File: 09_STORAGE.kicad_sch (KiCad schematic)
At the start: 0 parts

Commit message: updated schematics
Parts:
- added C901: 4.7uF, Capacitor_SMD:C_0603_1608Metric, symbol Device:C
- added C902: 220nF, Capacitor_SMD:C_0402_1005Metric, symbol Device:C
- added C903: 2.2uF, Capacitor_SMD:C_0603_1608Metric, symbol Device:C
- added C904, C906: 100nF, Capacitor_SMD:C_0402_1005Metric, symbol Device:C
- added C905: 1.0uF, Capacitor_SMD:C_0402_1005Metric, symbol Device:C
- added R901: 10k, Resistor_SMD:R_0402_1005Metric, symbol Device:R
- added R902, R903, R904, R905, R906, R907, R908, R909, R910: 47k, Resistor_SMD:R_0402_1005Metric, symbol Device:R
- added U1: EMMC64G-TB9F-06011, symbol sportwatch_custom:EMMC64G-TB9F-06011
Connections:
- new net: U1.A1 (NC), U1.A10 (NC), U1.A11 (NC), U1.A12 (NC), U1.A13 (NC), U1.A14 (NC), U1.A2 (NC), U1.A7 (RFU), U1.A8 (NC), U1.A9 (NC), U1.B1 (NC), U1.B10 (NC), U1.B11 (NC), U1.B12 (NC), U1.B13 (NC), U1.B14 (NC), U1.B7 (NC), U1.B8 (NC), U1.B9 (NC), U1.C1 (NC), U1.C10 (NC), U1.C11 (NC), U1.C12 (NC), U1.C13 (NC), U1.C14 (NC), U1.C3 (NC), U1.C5 (NC), U1.C7 (NC), U1.C8 (NC), U1.C9 (NC), U1.D1 (NC), U1.D12 (NC), U1.D13 (NC), U1.D14 (NC), U1.D2 (NC), U1.D3 (NC), U1.D4 (NC), U1.E1 (NC), U1.E10 (VSF), U1.E12 (NC), U1.E13 (NC), U1.E14 (NC), U1.E2 (NC), U1.E3 (NC), U1.E5 (RFU), U1.E8 (VSF), U1.E9 (VSF), U1.F1 (NC), U1.F10 (VSF), U1.F12 (NC), U1.F13 (NC), U1.F14 (NC), U1.F2 (NC), U1.F3 (NC), U1.G1 (NC), U1.G10 (VSF), U1.G12 (NC), U1.G13 (NC), U1.G14 (NC), U1.G2 (NC), U1.G3 (RFU), U1.H1 (NC), U1.H12 (NC), U1.H13 (NC), U1.H14 (NC), U1.H2 (NC), U1.H3 (NC), U1.J1 (NC), U1.J12 (NC), U1.J13 (NC), U1.J14 (NC), U1.J2 (NC), U1.J3 (NC), U1.K1 (NC), U1.K10 (VSF), U1.K12 (NC), U1.K13 (NC), U1.K14 (NC), U1.K2 (NC), U1.K3 (NC), U1.K6 (RFU), U1.K7 (RFU), U1.L1 (NC), U1.L12 (NC), U1.L13 (NC), U1.L14 (NC), U1.L2 (NC), U1.L3 (NC), U1.M1 (NC), U1.M10 (NC), U1.M11 (NC), U1.M12 (NC), U1.M13 (NC), U1.M14 (NC), U1.M2 (NC), U1.M3 (NC), U1.M7 (NC), U1.M8 (NC), U1.M9 (NC), U1.N1 (NC), U1.N10 (NC), U1.N11 (NC), U1.N12 (NC), U1.N13 (NC), U1.N14 (NC), U1.N3 (NC), U1.N6 (NC), U1.N7 (NC), U1.N8 (NC), U1.N9 (NC), U1.P1 (NC), U1.P10 (RFU), U1.P11 (NC), U1.P12 (NC), U1.P13 (NC), U1.P14 (NC), U1.P2 (NC), U1.P7 (RFU), U1.P8 (NC), U1.P9 (NC)
- new net: U1.A6 (VSS), U1.P6 (VSSQ)
- new net EMMC_CLK: U1.M6 (CLK)
- new net EMMC_CMD: R901.2, U1.M5 (CMD)
- new net EMMC_DAT0: R902.2, U1.A3 (DAT0)
- new net EMMC_DAT1: R903.2, U1.A4 (DAT1)
- new net EMMC_DAT2: R904.2, U1.A5 (DAT2)
- new net EMMC_DAT3: R905.2, U1.B2 (DAT3)
- new net EMMC_DAT4: R906.2, U1.B3 (DAT4)
- new net EMMC_DAT5: R907.2, U1.B4 (DAT5)
- new net EMMC_DAT6: R908.2, U1.B5 (DAT6)
- new net EMMC_DAT7: R909.2, U1.B6 (DAT7)
- new net EMMC_RST_N: R910.2, U1.K5 (~{RST_n})
- new net EMMC_VDDI: C905.1, C906.1, U1.C2 (VDDI)
- new net GND: C901.2, C902.2, C903.2, C904.2, C905.2, C906.2, U1.K8 (VSS)
- new net VOUT1_1V8: C903.1, C904.1, R901.1, R910.1, U1.C6 (VCCQ), U1.N4 (VCCQ), U1.P5 (VCCQ)
- new net VOUT2_3V0_PROVISIONAL: C901.1, C902.1, U1.E6 (VCC), U1.K9 (VCC)
- no-connect marks 0 -> 1
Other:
- note added: "09_STORAGE — 64 GB eMMC / APOLLO510B SDIO0 8-BIT — REV A"
- note added: "Add/tune a small CLK source-series resistor near Apollo during 01_APOLLO integration (22 ohm initial target); keep it physically at the host, not beside U1."
- note added: "Apollo510B documents SDIO0 up to 96 MHz / 96 MB/s. Therefore U1 is NOT operated in HS400; H5/DS is intentionally NC."
- note added: "Architecture: Apollo510B SDIO0 is reserved for this eMMC because SDIO0 supports the full 8-bit eMMC bus."
- note added: "C901/C902: VCC 4.7uF + 220nF. C903/C904: VCCQ 2.2uF + 100nF. C905/C906: VDDI 1uF + 100nF."
- note added: "EMMC_RST_N uses a normal Apollo GPIO; hardware reset is disabled by default in eMMC and must be enabled through EXT_CSD if used."
- note added: "Kingston states DAT1-DAT7 internal pull-ups are disconnected after entering wide-bus modes, so external biasing remains useful."
- note added: "Kingston's public datasheet calls for an external VDDI Creg but refers exact design values to a separate design guide; capacitor values use standard eMMC guidance."
- note added: "Place U1 close to Apollo. Route CLK/CMD/DAT0..7 as controlled-impedance short traces with a continuous reference plane; length/skew review occurs in PCB phase."
- note added: "R901=10k CMD pull-up; R902-R909=47k DAT pull-ups; R910=47k reset pull-up. Values are conservative eMMC/JEDEC-style biasing."
- note added: "RFU/VSF/NC balls remain unconnected exactly as Kingston requires. Footprint is intentionally still unassigned pending the dedicated FBGA153 footprint audit."
- note added: "Reserve Apollo SDIF0 signals: DAT0..3 on GPIO84..87, CLK on GPIO88, DAT4..7 on GPIO156..159, CMD on GPIO160."
- note added: "U1 custom FBGA153 ball map verified against Kingston Table 9 before wiring."
- note added: "VCC = VOUT2_3V0_PROVISIONAL. Kingston allows 2.7-3.6 V; 3.0 V reduces load on the separate display 3.3 V rail."
- note added: "VCCQ = VOUT1_1V8. This keeps the complete SDIO0 bus in the 1.8 V I/O domain and preserves high-speed compatibility."
- note added: "VOUT rails and host labels are still local to this child sheet until final hierarchical integration."
- title: (none) -> Rev-A — 64 GB eMMC Storage

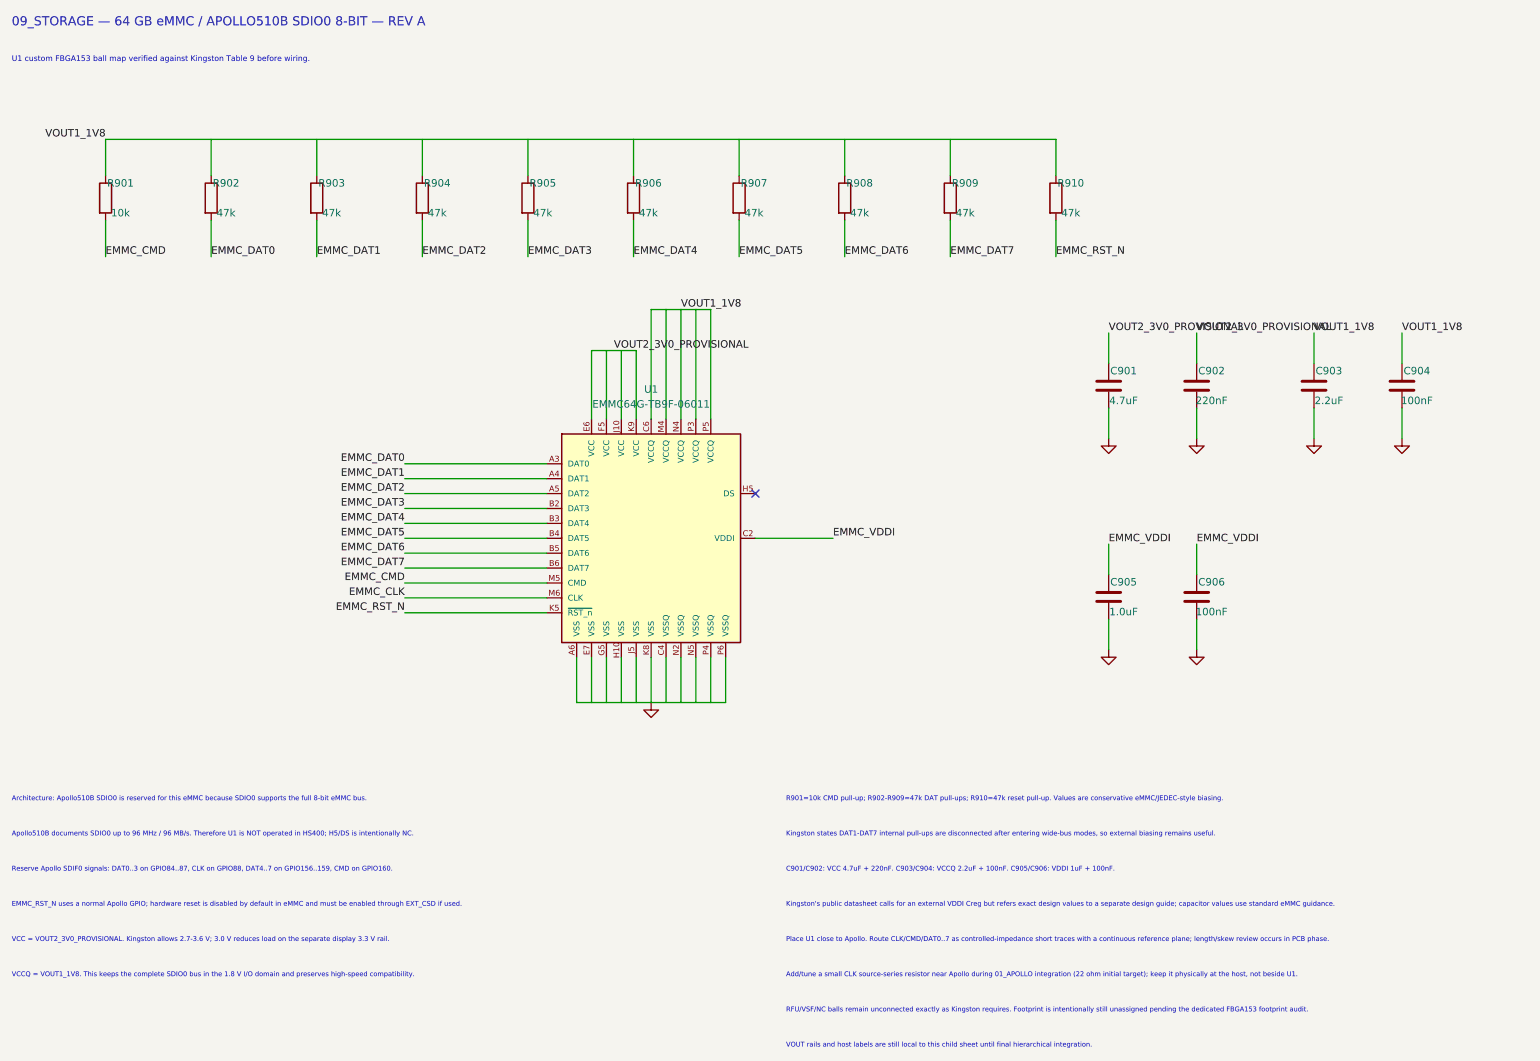
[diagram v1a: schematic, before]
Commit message: fixed schematics errors
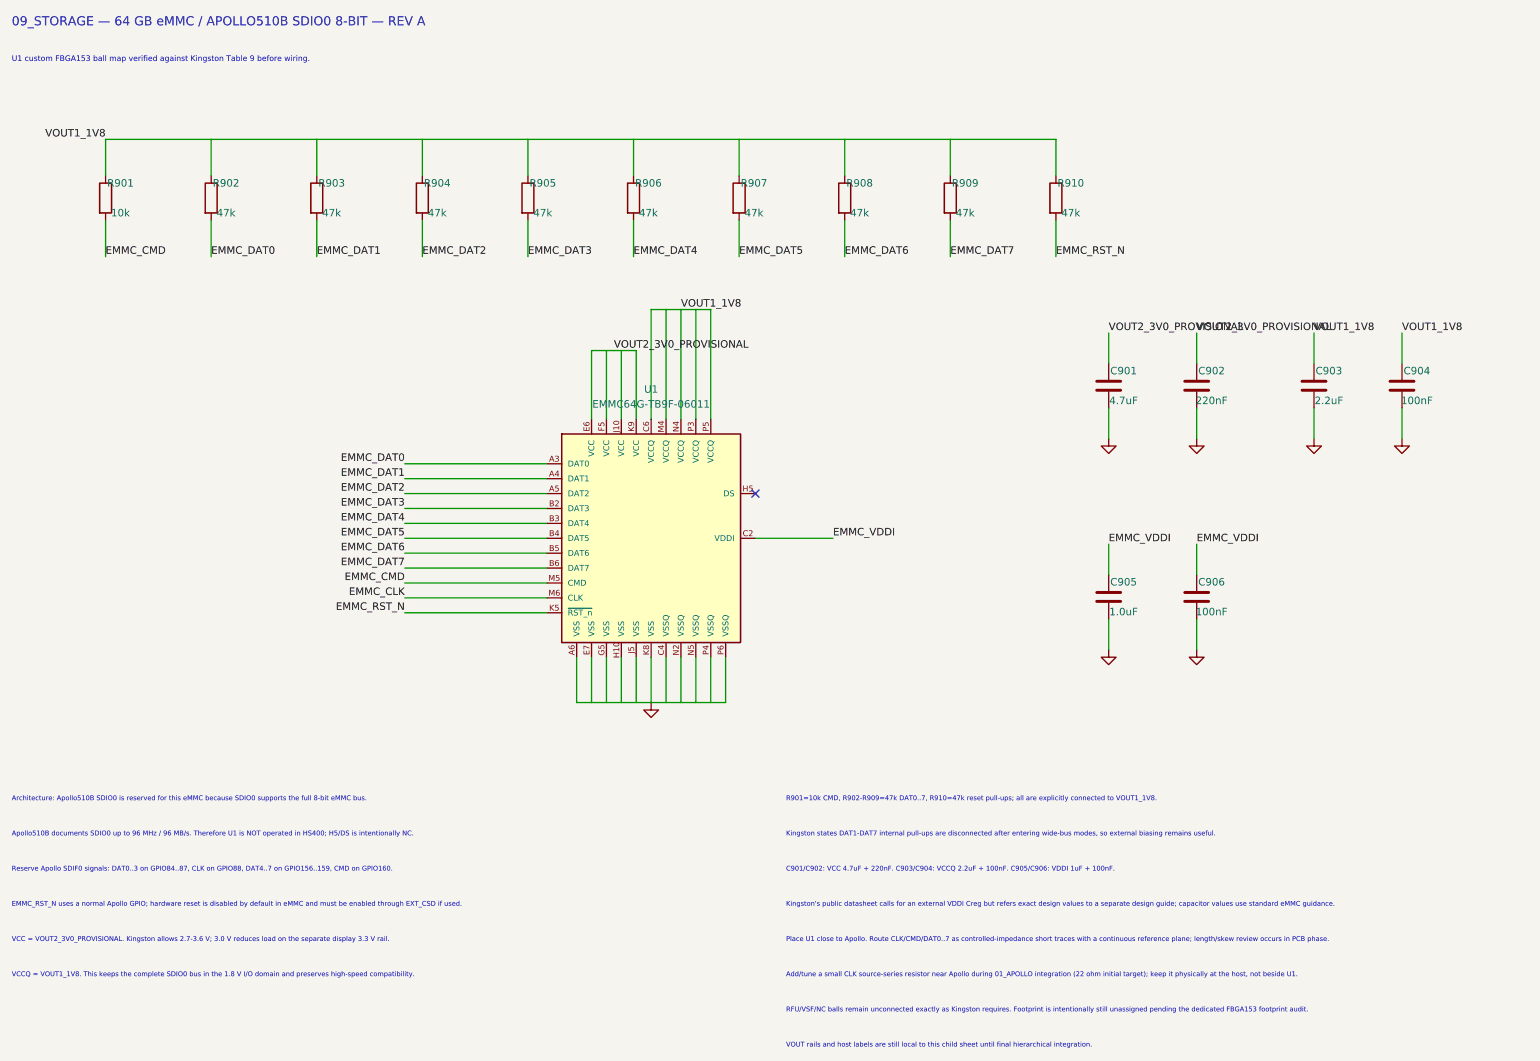
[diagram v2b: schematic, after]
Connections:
- net GND: now also U1.A6 (VSS), U1.C4 (VSSQ), U1.E7 (VSS), U1.G5 (VSS), U1.H10 (VSS), U1.J5 (VSS), U1.N2 (VSSQ), U1.N5 (VSSQ), U1.P4 (VSSQ), U1.P6 (VSSQ)
- net VOUT1_1V8: now also R902.1, R903.1, R904.1, R905.1, R906.1, R907.1, R908.1, R909.1, U1.M4 (VCCQ), U1.P3 (VCCQ)
- net VOUT2_3V0_PROVISIONAL: now also U1.F5 (VCC), U1.J10 (VCC)
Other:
- note added: "R901=10k CMD, R902-R909=47k DAT0..7, R910=47k reset pull-ups; all are explicitly connected to VOUT1_1V8."
- note removed: "R901=10k CMD pull-up; R902-R909=47k DAT pull-ups; R910=47k reset pull-up. Values are conservative eMMC/JEDEC-style biasing."
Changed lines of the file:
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@@
 		)
 	)
-	(text "R901=10k CMD pull-up; R902-R909=47k DAT pull-ups; R910=47k reset pull-up. Values are conservative eMMC/JEDEC-style biasing."
+	(text "R901=10k CMD, R902-R909=47k DAT0..7, R910=47k reset pull-ups; all are explicitly connected to VOUT1_1V8."
 		(exclude_from_sim no)
 		(at 150 145 0)
@@
 	(wire
 		(pts
-			(xy 114.3 128) (xy 139.7 128)
+			(xy 114.3 128) (xy 116.84 128)
+		)
+		(stroke
+			(width 0)
+			(type default)
+		)
+	)
+	(wire
+		(pts
+			(xy 116.84 128) (xy 119.38 128)
+		)
+		(stroke
+			(width 0)
+			(type default)
+		)
+	)
+	(wire
+		(pts
+			(xy 119.38 128) (xy 121.92 128)
+		)
+		(stroke
+			(width 0)
+			(type default)
+		)
+	)
+	(wire
+		(pts
+			(xy 121.92 128) (xy 124.46 128)
+		)
+		(stroke
+			(width 0)
+			(type default)
+		)
+	)
+	(wire
+		(pts
+			(xy 124.46 128) (xy 127 128)
+		)
+		(stroke
+			(width 0)
+			(type default)
+		)
+	)
+	(wire
+		(pts
+			(xy 127 128) (xy 129.54 128)
+		)
+		(stroke
+			(width 0)
+			(type default)
+		)
+	)
+	(wire
+		(pts
+			(xy 129.54 128) (xy 132.08 128)
+		)
+		(stroke
+			(width 0)
+			(type default)
+		)
+	)
+	(wire
+		(pts
+			(xy 132.08 128) (xy 134.62 128)
+		)
+		(stroke
+			(width 0)
+			(type default)
+		)
+	)
+	(wire
+		(pts
+			(xy 134.62 128) (xy 137.16 128)
+		)
+		(stroke
+			(width 0)
+			(type default)
+		)
+	)
+	(wire
+		(pts
+			(xy 137.16 128) (xy 139.7 128)
 		)
 		(stroke
@@
 	(wire
 		(pts
-			(xy 116.84 68) (xy 124.46 68)
+			(xy 116.84 68) (xy 119.38 68)
+		)
+		(stroke
+			(width 0)
+			(type default)
+		)
+	)
+	(wire
+		(pts
+			(xy 119.38 68) (xy 120.65 68)
+		)
+		(stroke
+			(width 0)
+			(type default)
+		)
+	)
+	(wire
+		(pts
+			(xy 120.65 68) (xy 121.92 68)
+		)
+		(stroke
+			(width 0)
+			(type default)
+		)
+	)
+	(wire
+		(pts
+			(xy 121.92 68) (xy 124.46 68)
 		)
 		(stroke
@@
 	(wire
 		(pts
-			(xy 127 61) (xy 137.16 61)
-		)
-		(stroke
-			(width 0)
-			(type default)
-		)
-	)
-	(wire
-		(pts
-			(xy 34 32) (xy 196 32)
-		)
-		(stroke
+			(xy 127 61) (xy 129.54 61)
+		)
+		(stroke
+			(width 0)
+			(type default)
+		)
+	)
+	(wire
+		(pts
+			(xy 129.54 61) (xy 132.08 61)
+		)
+		(stroke
+			(width 0)
+			(type default)
+		)
+	)
+	(wire
+		(pts
+			(xy 132.08 61) (xy 134.62 61)
+		)
+		(stroke
+			(width 0)
+			(type default)
+		)
+	)
+	(wire
+		(pts
+			(xy 134.62 61) (xy 137.16 61)
+		)
+		(stroke
+			(width 0)
+			(type default)
+		)
+	)
+	(wire
+		(pts
+			(xy 34 32) (xy 52 32)
+		)
+		(stroke
+			(width 0)
+			(type default)
+		)
+	)
+	(wire
+		(pts
+			(xy 52 32) (xy 70 32)
+		)
+		(stroke
+			(width 0)
+			(type default)
+		)
+	)
+	(wire
+		(pts
+			(xy 70 32) (xy 88 32)
+		)
+		(stroke
+			(width 0)
+			(type default)
+		)
+	)
+	(wire
+		(pts
+			(xy 88 32) (xy 106 32)
+		)
+		(stroke
+			(width 0)
+			(type default)
+		)
+	)
+	(wire
+		(pts
+			(xy 106 32) (xy 124 32)
+		)
+		(stroke
+			(width 0)
+			(type default)
+		)
+	)
+	(wire
+		(pts
+			(xy 124 32) (xy 142 32)
+		)
+		(stroke
+			(width 0)
+			(type default)
+		)
+	)
+	(wire
+		(pts
+			(xy 142 32) (xy 160 32)
+		)
+		(stroke
+			(width 0)
+			(type default)
+		)
+	)
+	(wire
+		(pts
+			(xy 160 32) (xy 178 32)
+		)
+		(stroke
+			(width 0)
+			(type default)
+		)
+	)
+	(wire
+		(pts
+			(xy 178 32) (xy 196 32)
+		)
+		(stroke

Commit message: refactor(kicad): integrate Rev-A hierarchy and libraries
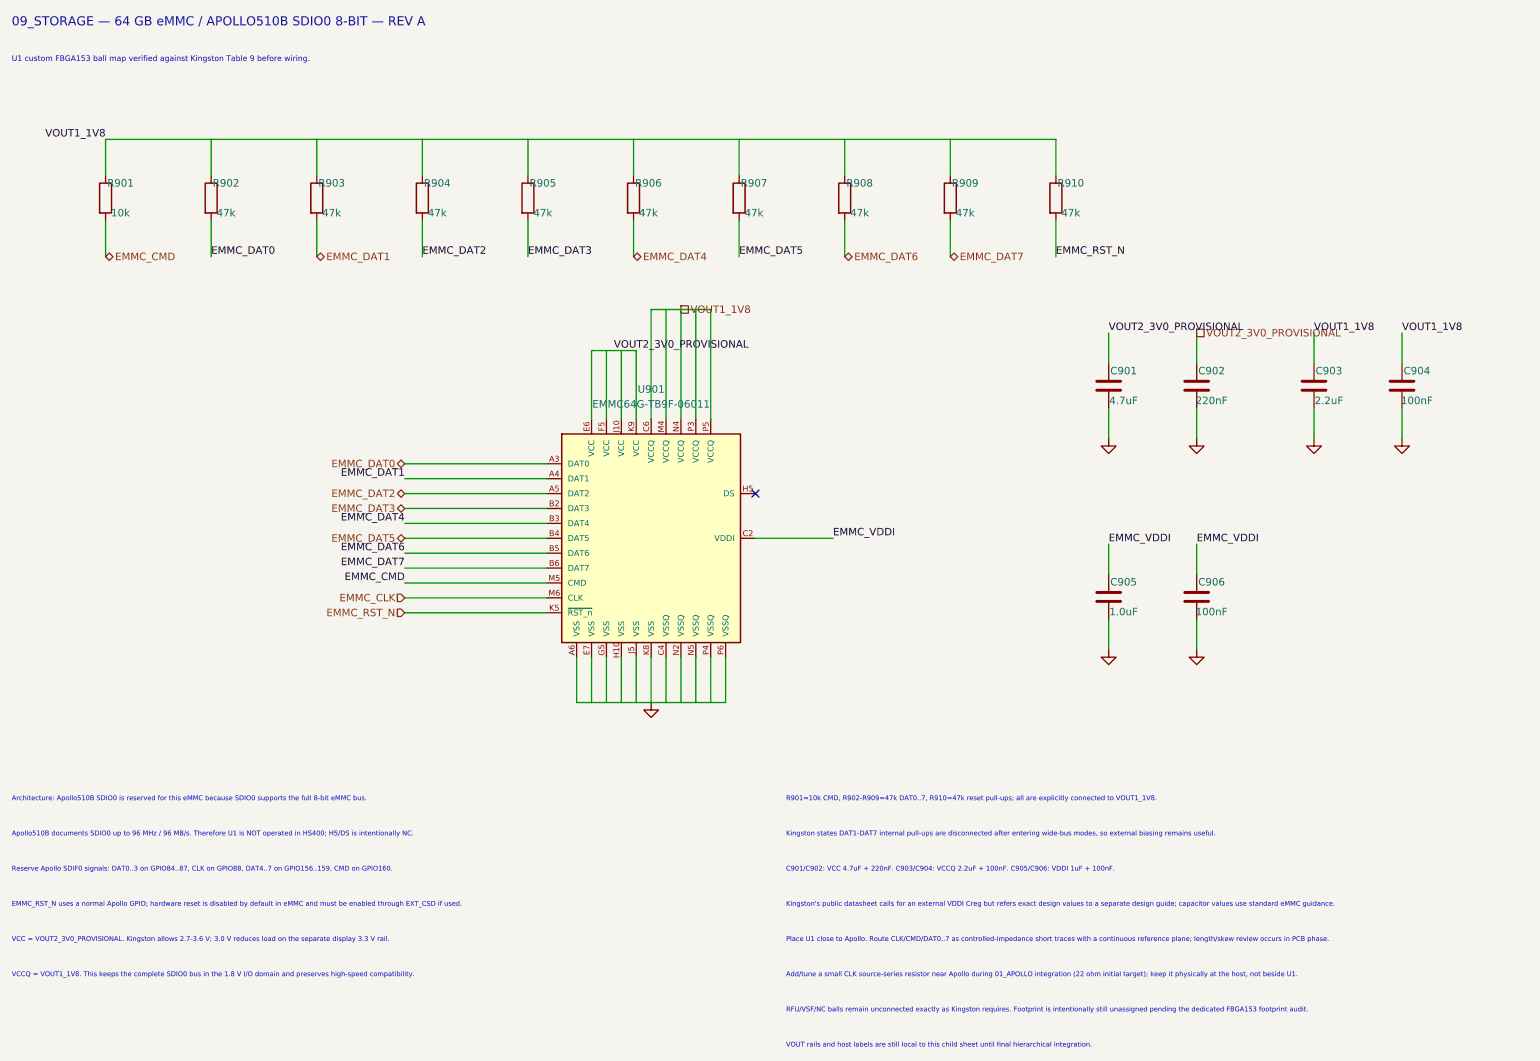
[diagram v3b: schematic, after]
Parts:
- renumbered U1 to U901
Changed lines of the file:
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@@
 		)
 	)
-	(label "VOUT2_3V0_PROVISIONAL"
+	(hierarchical_label "VOUT2_3V0_PROVISIONAL"
+		(shape passive)
 		(at 220 65 0)
 		(effects
@@
 		)
 	)
-	(label "EMMC_DAT4"
+	(hierarchical_label "EMMC_DAT4"
+		(shape bidirectional)
 		(at 124 52 0)
 		(effects
@@
 		)
 	)
-	(label "EMMC_DAT3"
+	(hierarchical_label "EMMC_DAT3"
+		(shape bidirectional)
 		(at 85 94.92 180)
 		(effects
@@
 		)
 	)
-	(label "EMMC_DAT2"
+	(hierarchical_label "EMMC_DAT2"
+		(shape bidirectional)
 		(at 85 92.38 180)
 		(effects
@@
 		)
 	)
-	(label "VOUT1_1V8"
+	(hierarchical_label "VOUT1_1V8"
+		(shape passive)
 		(at 132.08 61 0)
 		(effects
@@
 		)
 	)
-	(label "EMMC_DAT6"
+	(hierarchical_label "EMMC_DAT6"
+		(shape bidirectional)
 		(at 160 52 0)
 		(effects
@@
 		)
 	)
-	(label "EMMC_CMD"
+	(hierarchical_label "EMMC_CMD"
+		(shape bidirectional)
 		(at 34 52 0)
 		(effects
@@
 		)
 	)
-	(label "EMMC_DAT1"
+	(hierarchical_label "EMMC_DAT1"
+		(shape bidirectional)
 		(at 70 52 0)
 		(effects
@@
 		)
 	)
-	(label "EMMC_CLK"
+	(hierarchical_label "EMMC_CLK"
+		(shape input)
 		(at 85 110.16 180)
 		(effects
@@
 		)
 	)
-	(label "EMMC_DAT7"
+	(hierarchical_label "EMMC_DAT7"
+		(shape bidirectional)
 		(at 178 52 0)
 		(effects
@@
 		)
 	)
-	(label "EMMC_DAT5"
+	(hierarchical_label "EMMC_DAT5"
+		(shape bidirectional)
 		(at 85 100 180)
 		(effects
@@
 		)
 	)
-	(label "EMMC_RST_N"
+	(hierarchical_label "EMMC_RST_N"
+		(shape input)
 		(at 85 112.7 180)
 		(effects
@@
 		)
 	)
-	(label "EMMC_DAT0"
+	(hierarchical_label "EMMC_DAT0"
+		(shape bidirectional)
 		(at 85 87.3 180)
 		(effects
@@
 		(dnp no)
 		(fields_autoplaced yes)
-		(property "Reference" "U1"
+		(property "Reference" "U901"
 			(at 127 74.6 0)
 			(show_name no)
@@
 			(project "sportwatch_revA"
 				(path "/063f9d99-6c07-44cf-ba32-e33897e06972/a2d513ee-2f0e-4cad-81f9-7e29d5a45fba"
-					(reference "U1")
+					(reference "U901")
 					(unit 1)
 				)
@@
 			(project "09_STORAGE"
 				(path "/e1def6b6-01b4-4b57-bf23-17fd4247972f"
-					(reference "U1")
+					(reference "U901")
 					(unit 1)
 				)

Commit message: fix(kicad): correct PPG tri-state and eMMC hidden pins
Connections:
- now unconnected: U901.A1 (NC), U901.A10 (NC), U901.A11 (NC), U901.A12 (NC), U901.A13 (NC), U901.A14 (NC), U901.A2 (NC), U901.A7 (RFU), U901.A8 (NC), U901.A9 (NC), U901.B1 (NC), U901.B10 (NC), U901.B11 (NC), U901.B12 (NC), U901.B13 (NC), U901.B14 (NC), U901.B7 (NC), U901.B8 (NC), U901.B9 (NC), U901.C1 (NC), U901.C10 (NC), U901.C11 (NC), U901.C12 (NC), U901.C13 (NC), U901.C14 (NC), U901.C3 (NC), U901.C5 (NC), U901.C7 (NC), U901.C8 (NC), U901.C9 (NC), U901.D1 (NC), U901.D12 (NC), U901.D13 (NC), U901.D14 (NC), U901.D2 (NC), U901.D3 (NC), U901.D4 (NC), U901.E1 (NC), U901.E10 (VSF), U901.E12 (NC), U901.E13 (NC), U901.E14 (NC), U901.E2 (NC), U901.E3 (NC), U901.E5 (RFU), U901.E8 (VSF), U901.E9 (VSF), U901.F1 (NC), U901.F10 (VSF), U901.F12 (NC), U901.F13 (NC), U901.F14 (NC), U901.F2 (NC), U901.F3 (NC), U901.G1 (NC), U901.G10 (VSF), U901.G12 (NC), U901.G13 (NC), U901.G14 (NC), U901.G2 (NC), U901.G3 (RFU), U901.H1 (NC), U901.H12 (NC), U901.H13 (NC), U901.H14 (NC), U901.H2 (NC), U901.H3 (NC), U901.J1 (NC), U901.J12 (NC), U901.J13 (NC), U901.J14 (NC), U901.J2 (NC), U901.J3 (NC), U901.K1 (NC), U901.K10 (VSF), U901.K12 (NC), U901.K13 (NC), U901.K14 (NC), U901.K2 (NC), U901.K3 (NC), U901.K6 (RFU), U901.K7 (RFU), U901.L1 (NC), U901.L12 (NC), U901.L13 (NC), U901.L14 (NC), U901.L2 (NC), U901.L3 (NC), U901.M1 (NC), U901.M10 (NC), U901.M11 (NC), U901.M12 (NC), U901.M13 (NC), U901.M14 (NC), U901.M2 (NC), U901.M3 (NC), U901.M7 (NC), U901.M8 (NC), U901.M9 (NC), U901.N1 (NC), U901.N10 (NC), U901.N11 (NC), U901.N12 (NC), U901.N13 (NC), U901.N14 (NC), U901.N3 (NC), U901.N6 (NC), U901.N7 (NC), U901.N8 (NC), U901.N9 (NC), U901.P1 (NC), U901.P10 (RFU), U901.P11 (NC), U901.P12 (NC), U901.P13 (NC), U901.P14 (NC), U901.P2 (NC), U901.P7 (RFU), U901.P8 (NC), U901.P9 (NC)

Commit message: feat(kicad): assign and audit Rev-A footprints
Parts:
- U901: footprint (none) -> sportwatch_custom:FBGA-153_8.0x8.5mm_Layout14x14_P0.5mm
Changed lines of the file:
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@@
 			)
 		)
-		(property "Footprint" ""
+		(property "Footprint" "sportwatch_custom:FBGA-153_8.0x8.5mm_Layout14x14_P0.5mm"
 			(at 127 100 0)
 			(hide yes)
